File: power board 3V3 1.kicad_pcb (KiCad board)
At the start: 2 copper layers, 26 parts, among them J1 Conn_01x15_Pin, J2 Conn_01x15_Pin, Q1 NMOS - HL3400A, Q2 PMOS - SI2301, Q3 PMOS - SI2301, U1 TP4056-42-ESOP8, U2 HT7533-1-SOT89, U3 LM358DR

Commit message: Ugh
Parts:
- removed J2: Conn_01x15_Pin, Connector_PinHeader_2.54mm:PinHeader_1x15_P2.54mm_Vertical
- J1: value Conn_01x15_Pin -> Conn_02x15_Odd_Even; footprint Connector_PinHeader_2.54mm:PinHeader_1x15_P2.54mm_Vertical -> Connector_PinHeader_2.54mm:PinHeader_2x15_P2.54mm_Vertical
- moved R3 96.3 mm to (156.4, 100.6), turned to 0 degrees
- moved D2 93.0 mm to (162.3, 102.5), turned to 0 degrees
- moved C1 92.5 mm to (153.9, 98.8)
- moved C2 89.6 mm to (153.9, 100.6), turned to 0 degrees
- moved D1 89.2 mm to (162.3, 99.5), turned to 0 degrees
- moved R1 88.5 mm to (153.9, 105.8)
- moved R2 87.2 mm to (156.4, 98.8)
- moved R6 85.9 mm to (156.4, 105.8)
- moved U1 85.7 mm to (148.5, 101.3)
- moved U2 84.2 mm to (156.1, 109.8), turned to 0 degrees
- moved R5 84.0 mm to (156.4, 104.1)
- moved D3 77.6 mm to (161.9, 105.3), turned to 0 degrees
- moved C3 77.3 mm to (153.9, 102.3), turned to 0 degrees
- moved C4 75.9 mm to (153.9, 104.1), turned to 0 degrees
- moved R8 75.7 mm to (158.8, 100.6), turned to 0 degrees
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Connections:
- J1 pad 1: /+BATT2 -> +BATT
- J1 pad 10: /-BATT1 -> /+BATT2
- J1 pad 11: +BATT -> /-BATT1
- J1 pad 12: /BATT2CHRG1 -> -BATT
- J1 pad 13: +5V -> +BATT
- J1 pad 14: +BATT -> /+RPP2
- J1 pad 15: +BATT -> -BATT
- J1 pad 2: /SELECTOR OUT1 -> /+BATT_UVLO
- J1 pad 3: /+BATT_UVLO -> +BATT
- J1 pad 4: +5V -> /UVLO ON2
- J1 pad 5: /VREGOUT1 -> +5V
- J1 pad 6: /SELECTOR OUT2 -> /POW CHRGR2
- J1 pad 7: /RPPGND1 -> /BATT2CHRG1
- J1 pad 8: -BATT -> +BATT

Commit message: Next is just silk screen labelling and ask Si Teng if Im retarded
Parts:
- J1: value Conn_02x15_Odd_Even -> Conn_02x14_Odd_Even; footprint Connector_PinHeader_2.54mm:PinHeader_2x15_P2.54mm_Vertical -> Connector_PinHeader_2.54mm:PinHeader_2x14_P2.54mm_Vertical
- moved R1 30.1 mm to (161.1, 76.7)
- moved D2 29.9 mm to (161.4, 72.7), turned to 90 degrees
- moved D1 26.9 mm to (164.1, 72.7), turned to 90 degrees
- moved U1 26.4 mm to (156.1, 76.0)
- moved R3 25.8 mm to (150.9, 75.4), turned to 180 degrees
- moved C1 25.1 mm to (150.9, 73.9)
- moved Q1 24.6 mm to (147.2, 76.2), turned to 180 degrees
- moved R2 23.9 mm to (161.1, 75.4)
- moved C2 22.9 mm to (150.9, 77.9), turned to 180 degrees
- moved R6 21.5 mm to (155.6, 84.3), turned to -90 degrees
- moved D4 21.3 mm to (146.0, 93.6), turned to -90 degrees
- moved U3 20.5 mm to (157.5, 89.5), turned to -90 degrees
- moved Q3 19.8 mm to (147.0, 90.0), turned to 90 degrees
- moved R5 19.8 mm to (156.9, 84.3), turned to 90 degrees
- moved D3 18.9 mm to (161.1, 86.3), turned to 90 degrees
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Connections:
- BT1 pad 1: /FUSE2 -> /+BATT2
- J1 pad 10: /+BATT2 -> /POW CHRGR2
- J1 pad 11: /-BATT1 -> +BATT
- J1 pad 12: -BATT -> /+BATT_UVLO
- J1 pad 14: /+RPP2 -> /UVLO ON2
- J1 pad 15: -BATT -> /+BATT_UVLO
- J1 pad 16: /-RPP2 -> /UVLO2SEL2
- J1 pad 17: /RPPGND1 -> +5V
- J1 pad 18: GND -> /USB2SEL2
- J1 pad 19: /SELECTOR OUT2 -> /SELECTOR OUT1
- J1 pad 2: /+BATT_UVLO -> /+BATT2
- J1 pad 20: /VREG2 -> /SELECTOR OUT2
- J1 pad 21: /VREGOUT1 -> /SELECTOR OUT2
- J1 pad 22: +3V3 -> /VREG2
- J1 pad 23: +5V -> /VREGOUT1
- J1 pad 24: /USB2SEL2 -> +3V3
- J1 pad 25: /+BATT_UVLO -> -BATT
- J1 pad 26: /UVLO2SEL2 -> /-RPP2
- J1 pad 27: /SELECTOR OUT1 -> /-BATT1
- J1 pad 28: /SELECTOR OUT2 -> -BATT
- J1 pad 4: /UVLO ON2 -> /+RPP2
- J1 pad 5: +5V -> /RPPGND1
- J1 pad 6: /POW CHRGR2 -> GND
- J1 pad 9: +BATT -> +5V
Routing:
- net /POW CHRGR2: track 0.00 -> 54.0 mm, vias 0 -> 1
- net /-BATT1: track 0.00 -> 49.6 mm
- net /+BATT2: track 0.00 -> 45.5 mm
- net /UVLO ON2: track 0.00 -> 43.3 mm, vias 0 -> 1
- net /-RPP2: track 0.00 -> 30.0 mm, vias 0 -> 1
- net +BATT: track 0.00 -> 29.1 mm
- net GND: track 0.00 -> 26.8 mm, vias 0 -> 5
- net /BATT2CHRG1: track 0.00 -> 21.3 mm
- net /+BATT_UVLO: track 0.00 -> 21.0 mm
- net /VREG2: track 0.00 -> 14.3 mm
- net /SELECTOR OUT1: track 0.00 -> 12.2 mm
- net +5V: track 0.00 -> 11.1 mm
- net /USB2SEL2: track 0.00 -> 10.7 mm
- net /Vtest: track 0.00 -> 9.71 mm
- net /VREGOUT1: track 0.00 -> 9.29 mm
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- added copper zone on B.Cu, net GND
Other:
- board outline added: 70 x 92.5 mm

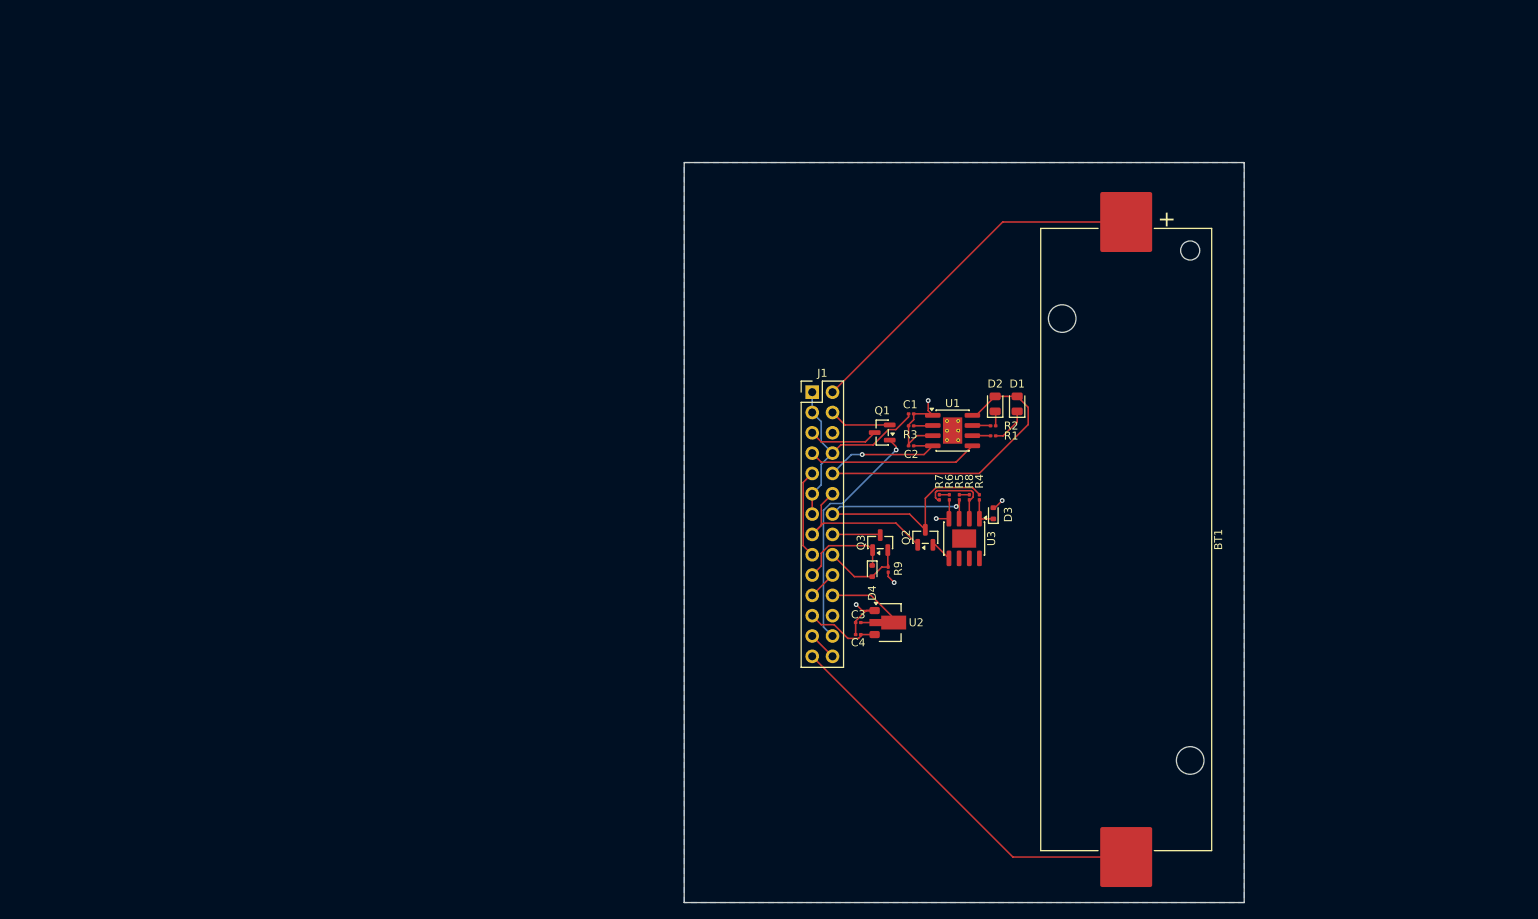
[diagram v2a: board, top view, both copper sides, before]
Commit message: Moved test pads
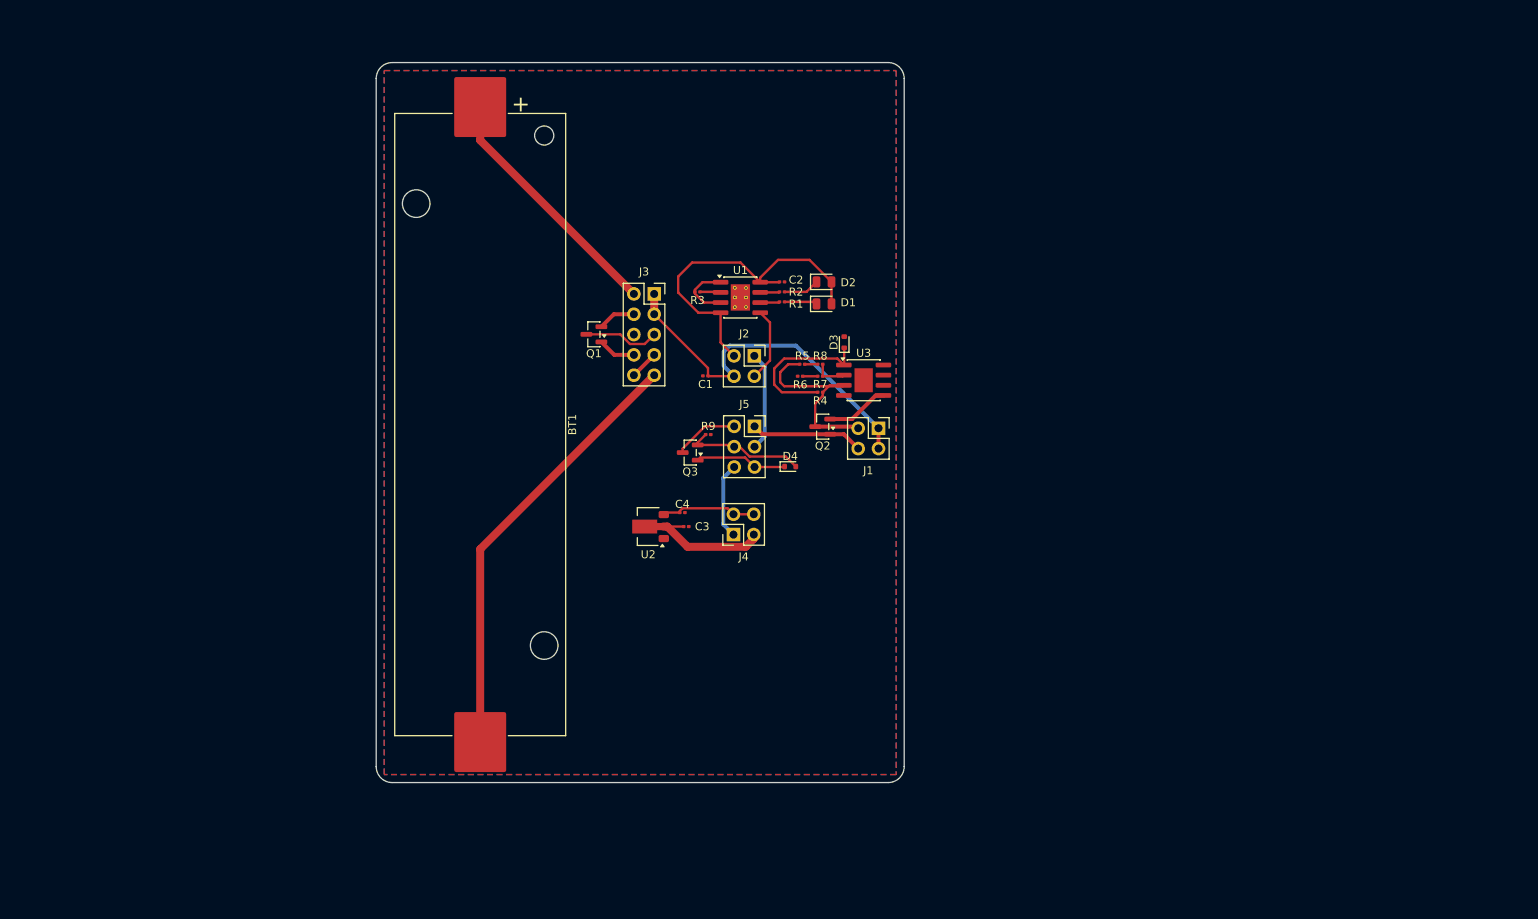
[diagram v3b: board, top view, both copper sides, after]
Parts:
- added J2: CHRGR TP, Connector_PinSocket_2.54mm:PinSocket_2x02_P2.54mm_Vertical, F.Cu at (131.3, 66.7)
- added J3: BATT & RPP TP, Connector_PinSocket_2.54mm:PinSocket_2x05_P2.54mm_Vertical, F.Cu at (118.8, 58.9)
- added J4: LDO TP, Connector_PinSocket_2.54mm:PinSocket_2x02_P2.54mm_Vertical, F.Cu at (128.7, 89.0)
- added J5: SRC CTRL TP, Connector_PinSocket_2.54mm:PinSocket_2x03_P2.54mm_Vertical, F.Cu at (131.3, 75.5)
- J1: value Conn_02x14_Odd_Even -> UVLO TP; footprint Connector_PinHeader_2.54mm:PinHeader_2x14_P2.54mm_Vertical -> Connector_PinSocket_2.54mm:PinSocket_2x02_P2.54mm_Vertical
- moved BT1 82.0 mm to (97.0, 75.2)
- moved Q1 38.1 mm to (111.2, 64.0)
- moved U2 32.5 mm to (118.0, 88.0), turned to 180 degrees
- moved R3 31.5 mm to (124.2, 58.7)
- moved U1 31.3 mm to (129.5, 59.4)
- moved R1 31.3 mm to (134.7, 59.9)
- moved R2 31.3 mm to (134.7, 58.7)
- moved D3 28.4 mm to (142.5, 65.0)
- moved R9 28.1 mm to (125.5, 76.5), turned to 0 degrees
- moved D1 27.2 mm to (140.0, 60.2), turned to 0 degrees
- moved C4 26.8 mm to (122.3, 86.2), turned to 0 degrees
- moved Q3 26.3 mm to (123.2, 78.8), turned to 180 degrees
- moved D2 26.3 mm to (140.0, 57.4), turned to 0 degrees
- moved C1 26.1 mm to (125.2, 69.2), turned to 180 degrees
- moved C2 26.1 mm to (134.7, 57.4), turned to 0 degrees
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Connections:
- C4 pad 1: /VREGOUT1 -> +3V3
- J1 pad 2: /+BATT2 -> /UVLO ON2
- J1 pad 4: /+RPP2 -> /+BATT_UVLO
- U2 pad 3: /VREGOUT1 -> +3V3
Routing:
- net /-RPP2: track 30.0 -> 4.73 mm, vias 1 -> 0
- net GND: track 26.8 -> 7.75 mm, vias 5 -> 0
- net /UVLO ON2: track 43.3 -> 25.4 mm, vias 1 -> 0
- net +BATT: track 29.1 -> 46.4 mm
- net /Vref: track 4.11 -> 19.5 mm
- net /+BATT2: track 45.5 -> 31.3 mm
- net /BATT2CHRG1: track 21.3 -> 9.25 mm
- net +3V3: track 0.00 -> 12.0 mm
- net /POW CHRGR2: track 54.0 -> 43.1 mm, vias 1 -> 0
- net /VREGOUT1: track 9.29 -> 0.00 mm
- net /+BATT_UVLO: track 21.0 -> 14.1 mm
- net /SELECTOR OUT2: track 3.59 -> 9.58 mm
- net /Vtest: track 9.71 -> 4.19 mm
- net /-BATT1: track 49.6 -> 54.9 mm
- net Net-(Q2-G): track 2.71 -> 7.87 mm
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- added copper zone on F.Cu, net GND
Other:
- board size 70 x 92.5 mm -> 66 x 90 mm

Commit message: PCB looks better now
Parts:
- BT1: footprint Battery:BatteryHolder_Keystone_1042_1x18650 -> Connector_PinHeader_2.54mm:PinHeader_1x02_P2.54mm_Vertical
- moved D4 76.1 mm to (60.9, 66.8)
- moved J2 75.1 mm to (56.3, 61.9)
- moved C1 71.4 mm to (53.8, 68.3), turned to -90 degrees
- moved Q1 64.2 mm to (48.5, 77.5)
- moved J3 64.1 mm to (56.3, 73.4)
- moved J5 63.6 mm to (68.0, 70.0)
- moved Q3 62.3 mm to (61.4, 71.2), turned to 0 degrees
- moved R9 62.2 mm to (64.1, 66.8)
- moved D1 61.3 mm to (79.0, 53.9), turned to 180 degrees
- moved D2 61.0 mm to (79.0, 56.7), turned to 180 degrees
- moved J4 61.0 mm to (68.2, 81.1), turned to 0 degrees
- moved Q2 59.4 mm to (80.5, 73.7)
- moved U1 56.7 mm to (73.0, 62.4)
- moved R3 56.6 mm to (67.7, 61.7)
- moved R1 56.3 mm to (78.5, 62.9)
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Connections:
- C2 pad 1: /POW CHRGR2 -> +5V
- D1 pad 2: /POW CHRGR2 -> +5V
- D2 pad 2: /POW CHRGR2 -> +5V
- J2 pad 2: /POW CHRGR2 -> +5V
- U1 pad 4: /POW CHRGR2 -> +5V
- U1 pad 8: /POW CHRGR2 -> +5V
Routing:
- net +5V: track 12.4 -> 67.4 mm
- net /POW CHRGR2: track 43.1 -> 0.00 mm
- net /+BATT_UVLO: track 14.1 -> 50.3 mm
- net /-BATT1: track 54.9 -> 18.7 mm
- net Net-(Q2-G): track 7.87 -> 28.0 mm
- net /+BATT2: track 31.3 -> 11.8 mm
- net +BATT: track 46.4 -> 64.2 mm
- net /Vref: track 19.5 -> 4.45 mm
- net /RPPGND1: track 9.47 -> 21.0 mm, vias 0 -> 1
- net /BATT2CHRG1: track 9.25 -> 19.9 mm
- net Net-(D1-K): track 4.10 -> 14.2 mm
- net /UVLO ON2: track 25.4 -> 33.6 mm, vias 0 -> 3
- net /SELECTOR OUT1: track 11.5 -> 17.8 mm
- net +3V3: track 12.0 -> 17.4 mm
- net /UVLO2SEL2: track 8.09 -> 3.59 mm
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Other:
- board size 66 x 90 mm -> 63 x 36 mm

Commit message: Routing fixed
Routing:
- net GND: track 7.11 -> 34.1 mm, vias 0 -> 7
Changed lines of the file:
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@@
+	)
+	(segment
+		(start 76.1145 82.3205)
+		(end 75.3645 83.0705)
+		(width 0.3)
+		(layer "F.Cu")
+		(net 4)
+	)
+	(segment
+		(start 64.3825 66.775)
+		(end 65.5 66.775)
+		(width 0.3)
+		(layer "F.Cu")
+		(net 4)
+	)
+	(segment
+		(start 93.24 68.76)
+		(end 92 70)
+		(width 0.5)
+		(layer "F.Cu")
+		(net 4)
 	)
 	(segment
@@
 	)
 	(segment
+		(start 93.915 76.115)
+		(end 93.915 76.915)
+		(width 1)
+		(layer "F.Cu")
+		(net 4)
+	)
+	(segment
+		(start 75.3645 83.0705)
+		(end 75.3205 83.0705)
+		(width 0.3)
+		(layer "F.Cu")
+		(net 4)
+	)
+	(segment
+		(start 93.915 76.915)
+		(end 95 78)
+		(width 1)
+		(layer "F.Cu")
+		(net 4)
+	)
+	(segment
+		(start 66.4375 61.6875)
+		(end 66.425 61.675)
+		(width 0.3)
+		(layer "F.Cu")
+		(net 4)
+	)
+	(segment
+		(start 93.71 68.76)
+		(end 93.24 68.76)
+		(width 0.5)
+		(layer "F.Cu")
+		(net 4)
+	)
+	(segment
 		(start 70.475 60.4825)
 		(end 68.196282 60.4825)
@@
 	)
 	(segment
+		(start 75.3645 83.0705)
+		(end 76.1145 83.8205)
+		(width 0.3)
+		(layer "F.Cu")
+		(net 4)
+	)
+	(segment
+		(start 67.335 61.6875)
+		(end 66.4375 61.6875)
+		(width 0.3)
+		(layer "F.Cu")
+		(net 4)
+	)
+	(segment
 		(start 70.475 63.0225)
 		(end 68.326282 63.0225)
@@
 		(width 0.5)
 		(layer "F.Cu")
+		(net 4)
+	)
+	(via
+		(at 95 78)
+		(size 0.6)
+		(drill 0.3)
+		(layers "F.Cu" "B.Cu")
+		(net 4)
+	)
+	(via
+		(at 65.5 66.775)
+		(size 0.6)
+		(drill 0.3)
+		(layers "F.Cu" "B.Cu")
+		(net 4)
+	)
+	(via
+		(at 77.75 80)
+		(size 0.6)
+		(drill 0.3)
+		(layers "F.Cu" "B.Cu")
+		(net 4)
+	)
+	(via
+		(at 66.425 61.675)
+		(size 0.6)
+		(drill 0.3)
+		(layers "F.Cu" "B.Cu")
+		(net 4)
+	)
+	(via
+		(at 79.5 59)
+		(size 0.6)
+		(drill 0.3)
+		(layers "F.Cu" "B.Cu")
+		(net 4)
+	)
+	(via
+		(at 75.3645 83.0705)
+		(size 0.6)
+		(drill 0.3)
+		(layers "F.Cu" "B.Cu")
+		(net 4)
+	)
+	(via
+		(at 92 70)
+		(size 0.6)
+		(drill 0.3)
+		(layers "F.Cu" "B.Cu")
+		(net 4)
+	)
+	(segment
+		(start 66.425 61.675)
+		(end 69.1 59)
+		(width 0.3)
+		(layer "B.Cu")
+		(net 4)
+	)
+	(segment
+		(start 69.1 59)
+		(end 79.5 59)
+		(width 0.3)
+		(layer "B.Cu")
+		(net 4)
+	)
+	(segment
+		(start 77.75 80.685)
+		(end 77.75 80)
+		(width 0.3)
+		(layer "B.Cu")
+		(net 4)
+	)
+	(segment
+		(start 75.3645 83.0705)
+		(end 77.75 80.685)
+		(width 0.3)
+		(layer "B.Cu")
 		(net 4)
 	)
@@
 		(polygon
 			(pts
-				(xy 40 53) (xy 101 53) (xy 101 87) (xy 40 87)
+				(xy 40 53) (xy 40 87) (xy 101 87) (xy 101 53)
 			)
 		)
